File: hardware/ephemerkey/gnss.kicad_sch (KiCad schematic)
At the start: 14 parts, among them J6 U.FL

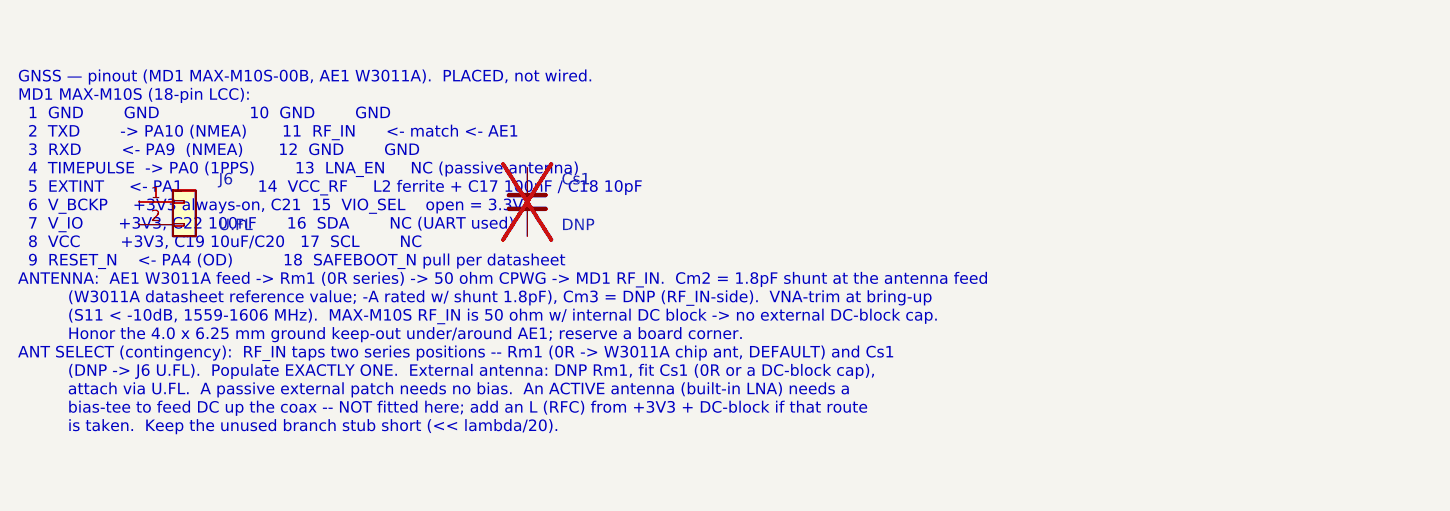
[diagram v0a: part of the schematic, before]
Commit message: hardware: on-board bias-tee for the U.FL path (active antenna, DNP)
Make the U.FL contingency active-antenna-ready without a respin. Reuse Cs1 as
the DC block and add a bias-tee, all DNP by default:
- L3: RF choke (+3V3 -> the Cs1<->J6 node; high-Z at L1, ~100nH or a ferrite)
- C33: +3V3 RF bypass to GND

For an active antenna: DNP Rm1, fit Cs1 as a DC-block cap (~10-33pF), fit L3 +
C33. DC rides +3V3 -> L3 -> U.FL centre -> coax -> antenna LNA; Cs1 blocks it
from RF_IN (which also has an internal DC block). Documented in the GNSS note +
DESIGN.md. make check-ephemerkey: 103 components, no dup refs, structure sound.

Co-Authored-By: Claude Opus 4.8 <noreply@anthropic.com>
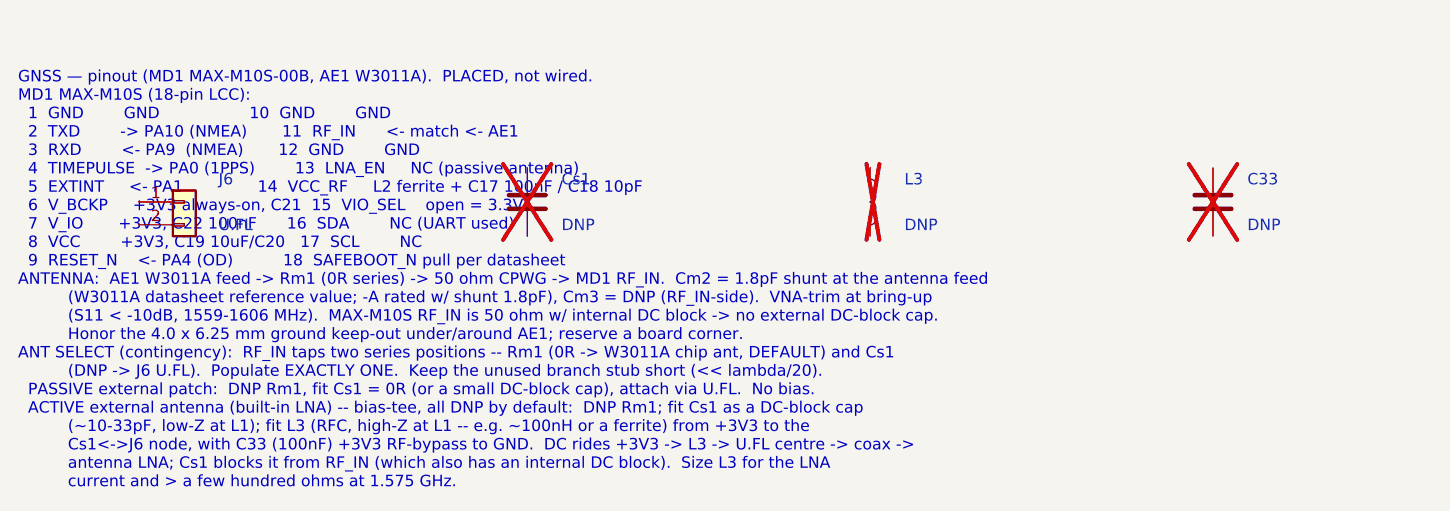
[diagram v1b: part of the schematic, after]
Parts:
- added C33: DNP, Capacitor_SMD:C_0402_1005Metric, symbol Device:C
- added L3: DNP, Inductor_SMD:L_0402_1005Metric, symbol Device:L
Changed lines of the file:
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@@
 		(company "EphemerKey Authors")
 	)
-	(text "GNSS — pinout (MD1 MAX-M10S-00B, AE1 W3011A).  PLACED, not wired.\nMD1 MAX-M10S (18-pin LCC):\n  1  GND        GND                  10  GND        GND\n  2  TXD        -> PA10 (NMEA)       11  RF_IN      <- match <- AE1\n  3  RXD        <- PA9  (NMEA)       12  GND        GND\n  4  TIMEPULSE  -> PA0 (1PPS)        13  LNA_EN     NC (passive antenna)\n  5  EXTINT     <- PA1               14  VCC_RF     L2 ferrite + C17 100nF / C18 10pF\n  6  V_BCKP     +3V3 always-on, C21  15  VIO_SEL    open = 3.3V\n  7  V_IO       +3V3, C22 100nF      16  SDA        NC (UART used)\n  8  VCC        +3V3, C19 10uF/C20   17  SCL        NC\n  9  RESET_N    <- PA4 (OD)          18  SAFEBOOT_N pull per datasheet\nANTENNA:  AE1 W3011A feed -> Rm1 (0R series) -> 50 ohm CPWG -> MD1 RF_IN.  Cm2 = 1.8pF shunt at the antenna feed\n          (W3011A datasheet reference value; -A rated w/ shunt 1.8pF), Cm3 = DNP (RF_IN-side).  VNA-trim at bring-up\n          (S11 < -10dB, 1559-1606 MHz).  MAX-M10S RF_IN is 50 ohm w/ internal DC block -> no external DC-block cap.\n          Honor the 4.0 x 6.25 mm ground keep-out under/around AE1; reserve a board corner.\nANT SELECT (contingency):  RF_IN taps two series positions -- Rm1 (0R -> W3011A chip ant, DEFAULT) and Cs1\n          (DNP -> J6 U.FL).  Populate EXACTLY ONE.  External antenna: DNP Rm1, fit Cs1 (0R or a DC-block cap),\n          attach via U.FL.  A passive external patch needs no bias.  An ACTIVE antenna (built-in LNA) needs a\n          bias-tee to feed DC up the coax -- NOT fitted here; add an L (RFC) from +3V3 + DC-block if that route\n          is taken.  Keep the unused branch stub short (<< lambda/20)."
+	(text "GNSS — pinout (MD1 MAX-M10S-00B, AE1 W3011A).  PLACED, not wired.\nMD1 MAX-M10S (18-pin LCC):\n  1  GND        GND                  10  GND        GND\n  2  TXD        -> PA10 (NMEA)       11  RF_IN      <- match <- AE1\n  3  RXD        <- PA9  (NMEA)       12  GND        GND\n  4  TIMEPULSE  -> PA0 (1PPS)        13  LNA_EN     NC (passive antenna)\n  5  EXTINT     <- PA1               14  VCC_RF     L2 ferrite + C17 100nF / C18 10pF\n  6  V_BCKP     +3V3 always-on, C21  15  VIO_SEL    open = 3.3V\n  7  V_IO       +3V3, C22 100nF      16  SDA        NC (UART used)\n  8  VCC        +3V3, C19 10uF/C20   17  SCL        NC\n  9  RESET_N    <- PA4 (OD)          18  SAFEBOOT_N pull per datasheet\nANTENNA:  AE1 W3011A feed -> Rm1 (0R series) -> 50 ohm CPWG -> MD1 RF_IN.  Cm2 = 1.8pF shunt at the antenna feed\n          (W3011A datasheet reference value; -A rated w/ shunt 1.8pF), Cm3 = DNP (RF_IN-side).  VNA-trim at bring-up\n          (S11 < -10dB, 1559-1606 MHz).  MAX-M10S RF_IN is 50 ohm w/ internal DC block -> no external DC-block cap.\n          Honor the 4.0 x 6.25 mm ground keep-out under/around AE1; reserve a board corner.\nANT SELECT (contingency):  RF_IN taps two series positions -- Rm1 (0R -> W3011A chip ant, DEFAULT) and Cs1\n          (DNP -> J6 U.FL).  Populate EXACTLY ONE.  Keep the unused branch stub short (<< lambda/20).\n  PASSIVE external patch:  DNP Rm1, fit Cs1 = 0R (or a small DC-block cap), attach via U.FL.  No bias.\n  ACTIVE external antenna (built-in LNA) -- bias-tee, all DNP by default:  DNP Rm1; fit Cs1 as a DC-block cap\n          (~10-33pF, low-Z at L1); fit L3 (RFC, high-Z at L1 -- e.g. ~100nH or a ferrite) from +3V3 to the\n          Cs1<->J6 node, with C33 (100nF) +3V3 RF-bypass to GND.  DC rides +3V3 -> L3 -> U.FL centre -> coax ->\n          antenna LNA; Cs1 blocks it from RF_IN (which also has an internal DC block).  Size L3 for the LNA\n          current and > a few hundred ohms at 1.575 GHz."
 		(exclude_from_sim no)
 		(at 12 137.92 0)
@@
 					(unit 1)
 				)
+			)
+		)
+	)
+	(symbol
+		(lib_id "Device:L")
+		(at 106.6800 152.4000 0)
+		(unit 1)
+		(exclude_from_sim no)
+		(in_bom yes)
+		(on_board yes)
+		(dnp yes)
+		(property "Reference" "L3"
+			(at 110.4900 149.8600 0)
+			(effects (font (size 1.27 1.27)) (justify left))
+		)
+		(property "Value" "DNP"
+			(at 110.4900 154.9400 0)
+			(effects (font (size 1.27 1.27)) (justify left))
+		)
+		(property "Footprint" "Inductor_SMD:L_0402_1005Metric"
+			(at 106.6800 152.4000 0)
+			(effects (font (size 1.27 1.27))) (hide yes)
+		)
+		(property "Datasheet" "~"
+			(at 106.6800 152.4000 0)
+			(effects (font (size 1.27 1.27))) (hide yes)
+		)
+		(pin "1")
+		(pin "2")
+		(instances
+			(project "ephemerkey"
+				(path "/ec65bc99-660e-415e-984b-47a2d6256a80/29c883c7-b979-475a-b755-896ca253f844"
+					(reference "L3")
+					(unit 1)
+				)
+			)
+		)
+	)
+	(symbol
+		(lib_id "Device:C")
+		(at 144.7800 152.4000 0)
+		(unit 1)
+		(exclude_from_sim no)
+		(in_bom yes)
+		(on_board yes)
+		(dnp yes)
+		(property "Reference" "C33"
+			(at 148.5900 149.8600 0)
+			(effects (font (size 1.27 1.27)) (justify left))
+		)
+		(property "Value" "DNP"
+			(at 148.5900 154.9400 0)
+			(effects (font (size 1.27 1.27)) (justify left))
+		)
+		(property "Footprint" "Capacitor_SMD:C_0402_1005Metric"
+			(at 144.7800 152.4000 0)
+			(effects (font (size 1.27 1.27))) (hide yes)
+		)
+		(property "Datasheet" "~"
+			(at 144.7800 152.4000 0)
+			(effects (font (size 1.27 1.27))) (hide yes)
+		)
+		(pin "1")
+		(pin "2")
+		(instances
+			(project "ephemerkey"
+				(path "/ec65bc99-660e-415e-984b-47a2d6256a80/29c883c7-b979-475a-b755-896ca253f844"
+					(reference "C33")
+					(unit 1)
+				)
